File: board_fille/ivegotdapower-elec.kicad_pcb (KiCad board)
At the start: 2 copper layers, 45 x 23 mm, 16 parts, among them J1 Conn_02x03_Odd_Even, J2 Conn_02x03_Odd_Even, U1 LM2596S-ADJ

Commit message: cleanup, finished design
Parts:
- JP1: value Jumper_NC_Dual -> SolderJumper_2_Open; footprint Jumper:SolderJumper-3_P1.3mm_Open_RoundedPad1.0x1.5mm -> Jumper:SolderJumper-2_P1.3mm_Open_TrianglePad1.0x1.5mm
- moved J2 76.6 mm to (141.8, 103.8), turned to 270 degrees
- moved JP1 74.1 mm to (104.2, 118.8), turned to 270 degrees
- moved C1 73.9 mm to (104.4, 105.4)
- moved J1 73.9 mm to (106.8, 112.8)
- moved C2 73.7 mm to (139.0, 114.4)
- moved C3 73.7 mm to (124.3, 103.5)
- moved D2 73.7 mm to (127.3, 102.7)
- moved F1 73.7 mm to (126.4, 105.8)
- moved L1 73.7 mm to (127.0, 113.8)
- moved R1 73.7 mm to (122.4, 105.8)
- moved R2 73.7 mm to (121.3, 102.5)
- moved R3 73.7 mm to (129.4, 104.8)
- moved R5 73.7 mm to (133.5, 102.5)
- moved R4 73.7 mm to (131.5, 104.7)
- moved U1 73.7 mm to (114.5, 108.4)
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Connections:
- JP1 pad 1: GND -> /on-off
- JP1 pad 2: Net-(JP1-Pad2) -> GND
- U1 pad 5: Net-(JP1-Pad2) -> /on-off
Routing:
- net /on-off: track 3.53 -> 19.8 mm, vias 0 -> 1
- net /Power_Output: track 20.2 -> 4.10 mm
- net Net-(JP1-Pad2): track 16.0 -> 0.00 mm, vias 2 -> 0
- net /Power_Input: track 18.8 -> 6.75 mm
- net GND: track 6.04 -> 0.00 mm, vias 0 -> 123
- net /voltage_measure: track 7.06 -> 8.80 mm, vias 0 -> 1
- added copper zone on F.Cu, net /Power_Input
- added copper zone on F.Cu, net /Power_Output
- added copper zone on B.Cu, net GND
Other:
- board size 45 x 23 mm -> 45 x 22 mm

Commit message: very small changes in fille
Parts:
- moved J1 0.28 mm to (107.0, 113.0)
- moved J2 0.28 mm to (142.0, 104.0)
- moved JP1 0.20 mm to (104.4, 118.8)
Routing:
- net /on-off: track 19.8 -> 18.5 mm

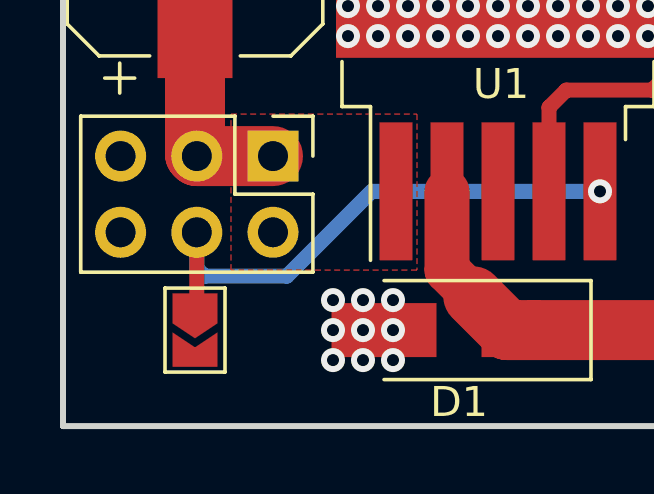
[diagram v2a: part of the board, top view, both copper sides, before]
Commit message: jumper error corrected
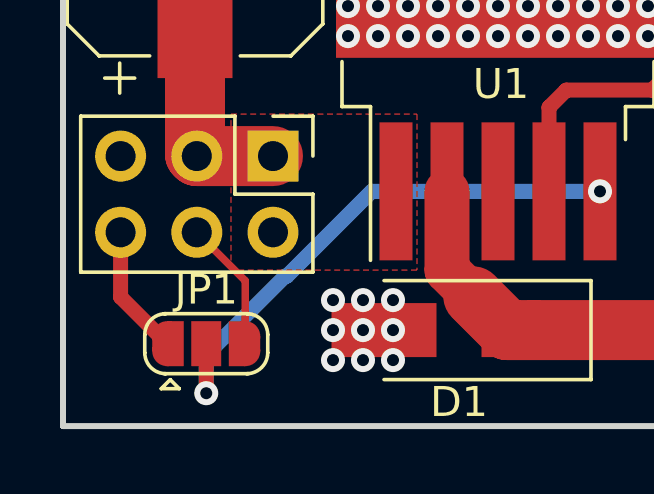
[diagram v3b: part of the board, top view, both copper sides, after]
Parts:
- JP1: value SolderJumper_2_Open -> SolderJumper_3_Open; footprint Jumper:SolderJumper-2_P1.3mm_Open_TrianglePad1.0x1.5mm -> Jumper:SolderJumper-3_P1.3mm_Open_RoundedPad1.0x1.5mm
- moved JP1 0.59 mm to (104.8, 119.3), turned to 0 degrees
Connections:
- JP1 pad 1: /on-off -> GND
- JP1 pad 2: GND -> Net-(JP1-Pad2)
- U1 pad 5: /on-off -> Net-(JP1-Pad2)
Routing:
- net Net-(JP1-Pad2): track 0.00 -> 18.3 mm, vias 0 -> 2
- net /on-off: track 18.5 -> 4.38 mm, vias 1 -> 0
- net GND: track 0.00 -> 4.36 mm
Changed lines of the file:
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@@
-(kicad_pcb (version 20171130) (host pcbnew 5.0.0)
+(kicad_pcb (version 20171130) (host pcbnew "(5.0.0-rc2-30-gcd5f727)")
   (general
     (thickness 1.6)
     (drawings 12)
-    (tracks 167)
+    (tracks 171)
     (zones 0)
     (modules 16)
-    (nets 10)
+    (nets 11)
   )
   (page A4)
@@
       (hpglpennumber 1)
       (hpglpenspeed 20)
-      (hpglpendiameter 15.000000)
+      (hpglpendiameter 15)
       (psnegative false)
       (psa4output false)
@@
   (net 8 "Net-(D1-Pad1)")
   (net 9 /on-off)
+  (net 10 "Net-(JP1-Pad2)")
   (net_class Default "Ceci est la Netclass par défaut."
     (clearance 0.2)
@@
     (add_net "Net-(D1-Pad1)")
     (add_net "Net-(D2-Pad2)")
+    (add_net "Net-(JP1-Pad2)")
+  )
+  (module Jumper:SolderJumper-3_P1.3mm_Open_RoundedPad1.0x1.5mm (layer F.Cu)
+    (at 104.775 119.253)
+    (descr "SMD Solder 3-pad Jumper, 1x1.5mm rounded Pads, 0.3mm gap, open")
+    (tags "solder jumper open")
+    (attr virtual)
+    (fp_text reference JP1 (at 0 -1.8) (layer F.SilkS)
+      (effects (font (size 1 1) (thickness 0.15)))
+    )
+    (fp_text value SolderJumper_3_Open (at 0 1.9) (layer F.Fab)
+      (effects (font (size 1 1) (thickness 0.15)))
+    )
+    (fp_line (start -1.2 1.2) (end -0.9 1.5) (layer F.SilkS) (width 0.12))
+    (fp_line (start -1.5 1.5) (end -0.9 1.5) (layer F.SilkS) (width 0.12))
+    (fp_line (start -1.2 1.2) (end -1.5 1.5) (layer F.SilkS) (width 0.12))
+    (fp_line (start -2.05 0.3) (end -2.05 -0.3) (layer F.SilkS) (width 0.12))
+    (fp_line (start 1.4 1) (end -1.4 1) (layer F.SilkS) (width 0.12))
+    (fp_line (start 2.05 -0.3) (end 2.05 0.3) (layer F.SilkS) (width 0.12))
+    (fp_line (start -1.4 -1) (end 1.4 -1) (layer F.SilkS) (width 0.12))
+    (fp_line (start -2.3 -1.25) (end 2.3 -1.25) (layer F.CrtYd) (width 0.05))
+    (fp_line (start -2.3 -1.25) (end -2.3 1.25) (layer F.CrtYd) (width 0.05))
+    (fp_line (start 2.3 1.25) (end 2.3 -1.25) (layer F.CrtYd) (width 0.05))
+    (fp_line (start 2.3 1.25) (end -2.3 1.25) (layer F.CrtYd) (width 0.05))
+    (fp_arc (start 1.35 -0.3) (end 2.05 -0.3) (angle -90) (layer F.SilkS) (width 0.12))
+    (fp_arc (start 1.35 0.3) (end 1.35 1) (angle -90) (layer F.SilkS) (width 0.12))
+    (fp_arc (start -1.35 0.3) (end -2.05 0.3) (angle -90) (layer F.SilkS) (width 0.12))
+    (fp_arc (start -1.35 -0.3) (end -1.35 -1) (angle -90) (layer F.SilkS) (width 0.12))
+    (pad 1 smd custom (at -1.3 0) (size 1 0.5) (layers F.Cu F.Mask)
+      (net 3 GND) (zone_connect 0)
+      (options (clearance outline) (anchor rect))
+      (primitives
+        (gr_circle (center 0 0.25) (end 0.5 0.25) (width 0))
+        (gr_circle (center 0 -0.25) (end 0.5 -0.25) (width 0))
+        (gr_poly (pts
+           (xy 0.55 -0.75) (xy 0 -0.75) (xy 0 0.75) (xy 0.55 0.75)) (width 0))
+      ))
+    (pad 3 smd custom (at 1.3 0) (size 1 0.5) (layers F.Cu F.Mask)
+      (net 9 /on-off) (zone_connect 0)
+      (options (clearance outline) (anchor rect))
+      (primitives
+        (gr_circle (center 0 0.25) (end 0.5 0.25) (width 0))
+        (gr_circle (center 0 -0.25) (end 0.5 -0.25) (width 0))
+        (gr_poly (pts
+           (xy -0.55 -0.75) (xy 0 -0.75) (xy 0 0.75) (xy -0.55 0.75)) (width 0))
+      ))
+    (pad 2 smd rect (at 0 0) (size 1 1.5) (layers F.Cu F.Mask)
+      (net 10 "Net-(JP1-Pad2)"))
   )
   (module Diode_SMD:D_SMA_Handsoldering (layer F.Cu)
@@
       (rotate (xyz 0 0 0))
     )
-  )
-  (module Jumper:SolderJumper-2_P1.3mm_Open_TrianglePad1.0x1.5mm (layer F.Cu)
-    (at 104.4 118.8 270)
-    (descr "SMD Solder Jumper, 1x1.5mm Triangular Pads, 0.3mm gap, open")
-    (tags "solder jumper open")
-    (attr virtual)
-    (fp_text reference JP1 (at 0 -2.6 270) (layer F.SilkS) hide
-      (effects (font (size 1 1) (thickness 0.15)))
-    )
-    (fp_text value SolderJumper_2_Open (at 0 1.9 270) (layer F.Fab)
-      (effects (font (size 1 1) (thickness 0.15)))
-    )
-    (fp_line (start -1.4 1) (end -1.4 -1) (layer F.SilkS) (width 0.12))
-    (fp_line (start 1.4 1) (end -1.4 1) (layer F.SilkS) (width 0.12))
-    (fp_line (start 1.4 -1) (end 1.4 1) (layer F.SilkS) (width 0.12))
-    (fp_line (start -1.4 -1) (end 1.4 -1) (layer F.SilkS) (width 0.12))
-    (fp_line (start -1.65 -1.25) (end 1.65 -1.25) (layer F.CrtYd) (width 0.05))
-    (fp_line (start -1.65 -1.25) (end -1.65 1.25) (layer F.CrtYd) (width 0.05))
-    (fp_line (start 1.65 1.25) (end 1.65 -1.25) (layer F.CrtYd) (width 0.05))
-    (fp_line (start 1.65 1.25) (end -1.65 1.25) (layer F.CrtYd) (width 0.05))
-    (pad 2 smd custom (at 0.725 0 270) (size 0.3 0.3) (layers F.Cu F.Mask)
-      (net 3 GND) (zone_connect 2)
-      (options (clearance outline) (anchor rect))
-      (primitives
-        (gr_poly (pts
-           (xy -0.65 -0.75) (xy 0.5 -0.75) (xy 0.5 0.75) (xy -0.65 0.75) (xy -0.15 0)
-) (width 0))
-      ))
-    (pad 1 smd custom (at -0.725 0 270) (size 0.3 0.3) (layers F.Cu F.Mask)
-      (net 9 /on-off) (zone_connect 0)
-      (options (clearance outline) (anchor rect))
-      (primitives
-        (gr_poly (pts
-           (xy -0.5 -0.75) (xy 0.5 -0.75) (xy 1 0) (xy 0.5 0.75) (xy -0.5 0.75)
-) (width 0))
-      ))
   )
   (module Connector_PinHeader_2.54mm:PinHeader_2x03_P2.54mm_Vertical (layer F.Cu)
@@
       (net 3 GND))
     (pad 5 smd rect (at -5.775 3.4 90) (size 4.6 1.1) (layers F.Cu F.Paste F.Mask)
-      (net 9 /on-off))
+      (net 10 "Net-(JP1-Pad2)"))
     (pad 4 smd rect (at -5.775 1.7 90) (size 4.6 1.1) (layers F.Cu F.Paste F.Mask)
       (net 2 "Net-(C3-Pad2)"))
@@
   (via (at 118.5 109) (size 0.8) (drill 0.4) (layers F.Cu B.Cu) (net 3))
   (via (at 119.5 109) (size 0.8) (drill 0.4) (layers F.Cu B.Cu) (net 3))
+  (segment (start 101.92 117.698) (end 103.475 119.253) (width 0.5) (layer F.Cu) (net 3))
+  (segment (start 101.92 115.54) (end 101.92 117.698) (width 0.5) (layer F.Cu) (net 3))
   (segment (start 129.375 105.8) (end 129.4 105.775) (width 1.5) (layer F.Cu) (net 4))
   (segment (start 127.425 105.8) (end 129.375 105.8) (width 1.5) (layer F.Cu) (net 4))
@@
   (segment (start 115.7 118.8) (end 114.8 118.8) (width 2) (layer F.Cu) (net 8))
   (segment (start 112.8 116.8) (end 113.675001 117.675001) (width 1.5) (layer F.Cu) (net 8))
-  (segment (start 104.46 116.742081) (end 104.717919 117) (width 0.5) (layer B.Cu) (net 9))
-  (segment (start 104.46 115.54) (end 104.46 116.742081) (width 0.5) (layer B.Cu) (net 9))
-  (via (at 117.9 114.175) (size 0.8) (drill 0.4) (layers F.Cu B.Cu) (net 9))
-  (segment (start 107.464002 117) (end 110.289002 114.175) (width 0.5) (layer B.Cu) (net 9))
-  (segment (start 110.289002 114.175) (end 117.9 114.175) (width 0.5) (layer B.Cu) (net 9))
-  (segment (start 104.717919 117) (end 107.464002 117) (width 0.5) (layer B.Cu) (net 9))
-  (segment (start 104.46 118.015) (end 104.4 118.075) (width 0.5) (layer F.Cu) (net 9))
-  (segment (start 104.46 115.54) (end 104.46 118.015) (width 0.5) (layer F.Cu) (net 9))
+  (segment (start 106.075 117.155) (end 104.46 115.54) (width 0.25) (layer F.Cu) (net 9))
+  (segment (start 106.075 119.253) (end 106.075 117.155) (width 0.25) (layer F.Cu) (net 9))
+  (via (at 117.9 114.175) (size 0.8) (drill 0.4) (layers F.Cu B.Cu) (net 10))
+  (segment (start 107.464002 117) (end 110.289002 114.175) (width 0.5) (layer B.Cu) (net 10))
+  (segment (start 110.289002 114.175) (end 117.9 114.175) (width 0.5) (layer B.Cu) (net 10))
+  (segment (start 107.464002 117) (end 107.409 117) (width 0.5) (layer B.Cu) (net 10))
+  (via (at 104.775 120.904) (size 0.8) (drill 0.4) (layers F.Cu B.Cu) (net 10))
+  (segment (start 104.775 119.634) (end 104.775 120.904) (width 0.5) (layer B.Cu) (net 10))
+  (segment (start 107.409 117) (end 104.775 119.634) (width 0.5) (layer B.Cu) (net 10))
+  (segment (start 104.775 120.904) (end 104.775 119.253) (width 0.5) (layer F.Cu) (net 10))
   (zone (net 3) (net_name GND) (layer F.Cu) (hatch edge 0.508)
     (connect_pads yes (clearance 0.508))

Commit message: update board_fille
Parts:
- removed JP1: SolderJumper_3_Open, Jumper:SolderJumper-3_P1.3mm_Open_RoundedPad1.0x1.5mm
- added R6: R, Resistor_SMD:R_0805_2012Metric_Pad1.15x1.40mm_HandSolder, B.Cu at (109.8, 112.7)
- R3, R4, R5: moved to B.Cu
- moved D2 6.46 mm to (133.8, 102.4)
- moved R3 4.41 mm to (133.8, 104.5)
- moved R5 3.70 mm to (129.8, 102.4)
- moved D1 2.72 mm to (110.5, 118.5)
- moved J1 0.60 mm to (107.0, 112.4)
- moved J2 0.60 mm to (142.0, 103.4)
- moved L1 0.45 mm to (126.8, 113.4)
- moved C2 0.40 mm to (139.0, 114.0)
- moved R4 0.38 mm to (131.8, 104.5)
- moved C1 0.10 mm to (104.4, 105.3)
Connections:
- U1 pad 5: Net-(JP1-Pad2) -> /on-off
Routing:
- net Net-(JP1-Pad2): track 18.3 -> 0.00 mm, vias 2 -> 0
- net /on-off: track 4.38 -> 14.1 mm, vias 0 -> 1
- net /Power_Output: track 4.10 -> 10.4 mm
- net GND: track 4.36 -> 0.00 mm
- net Net-(D2-Pad2): track 2.05 -> 0.00 mm, vias 0 -> 1
- net /voltage_measure: track 9.09 -> 10.8 mm, vias 1 -> 0
- net Net-(D1-Pad1): track 17.7 -> 18.3 mm
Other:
- board size 45 x 22 mm -> 44.5 x 20.3 mm
